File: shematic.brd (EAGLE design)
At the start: 99 x 50.5 mm, 15 parts, among them Y1 16MHZ

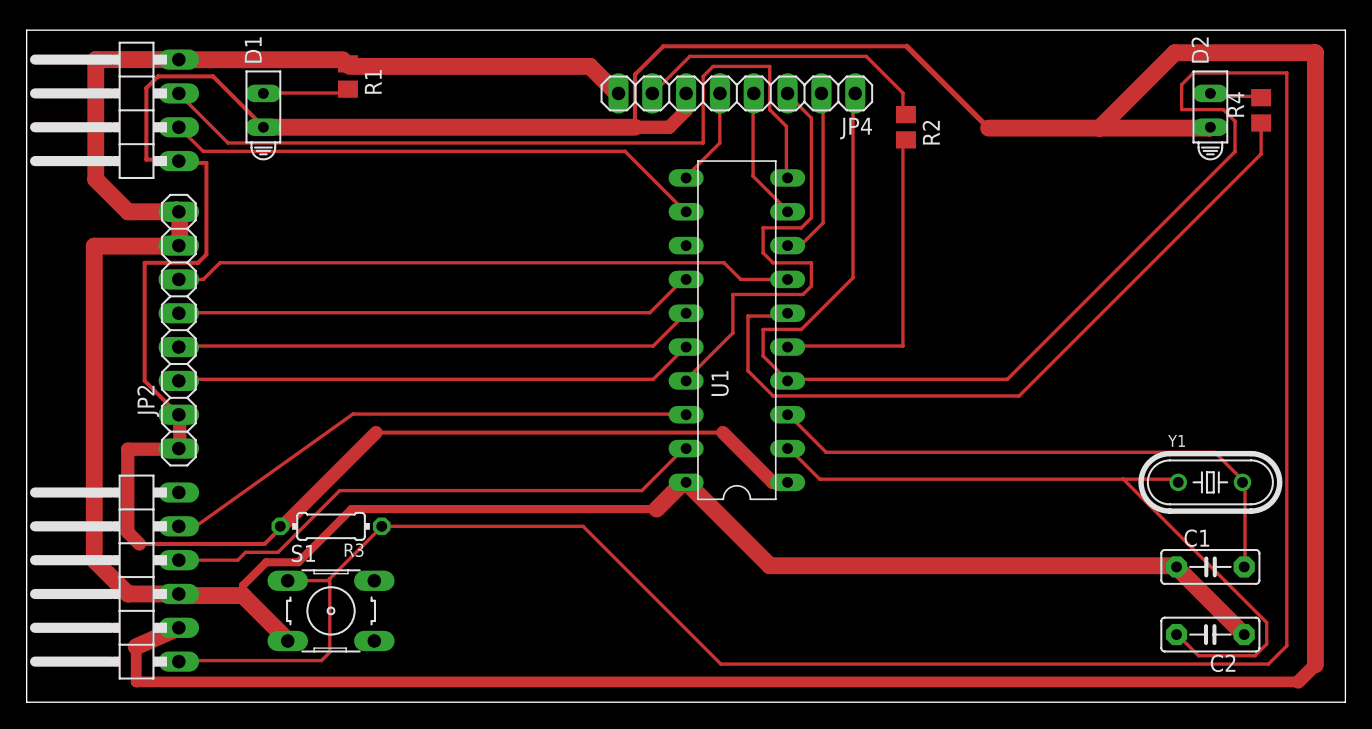
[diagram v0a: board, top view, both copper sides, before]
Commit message: set taller routes width
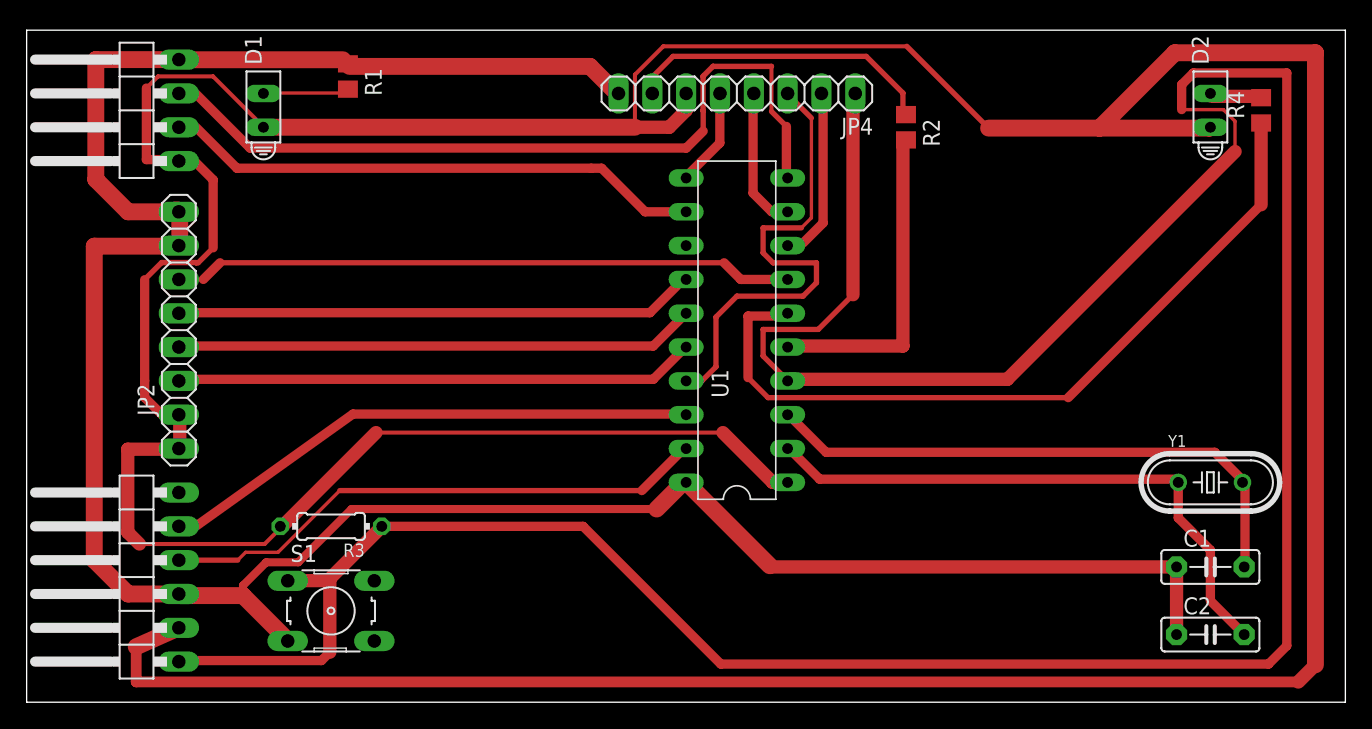
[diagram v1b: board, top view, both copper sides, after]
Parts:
- turned C2 to 0 degrees
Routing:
- net N$2: track 55.0 -> 43.9 mm
- net RC4: track 56.4 -> 59.0 mm
- net GND: track 190.2 -> 188.1 mm
- net DC: track 35.7 -> 36.7 mm
- net VPP: track 226.2 -> 226.9 mm
- net N$5: track 22.9 -> 23.6 mm
- net SDO: track 9.97 -> 10.7 mm

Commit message: fix some wires
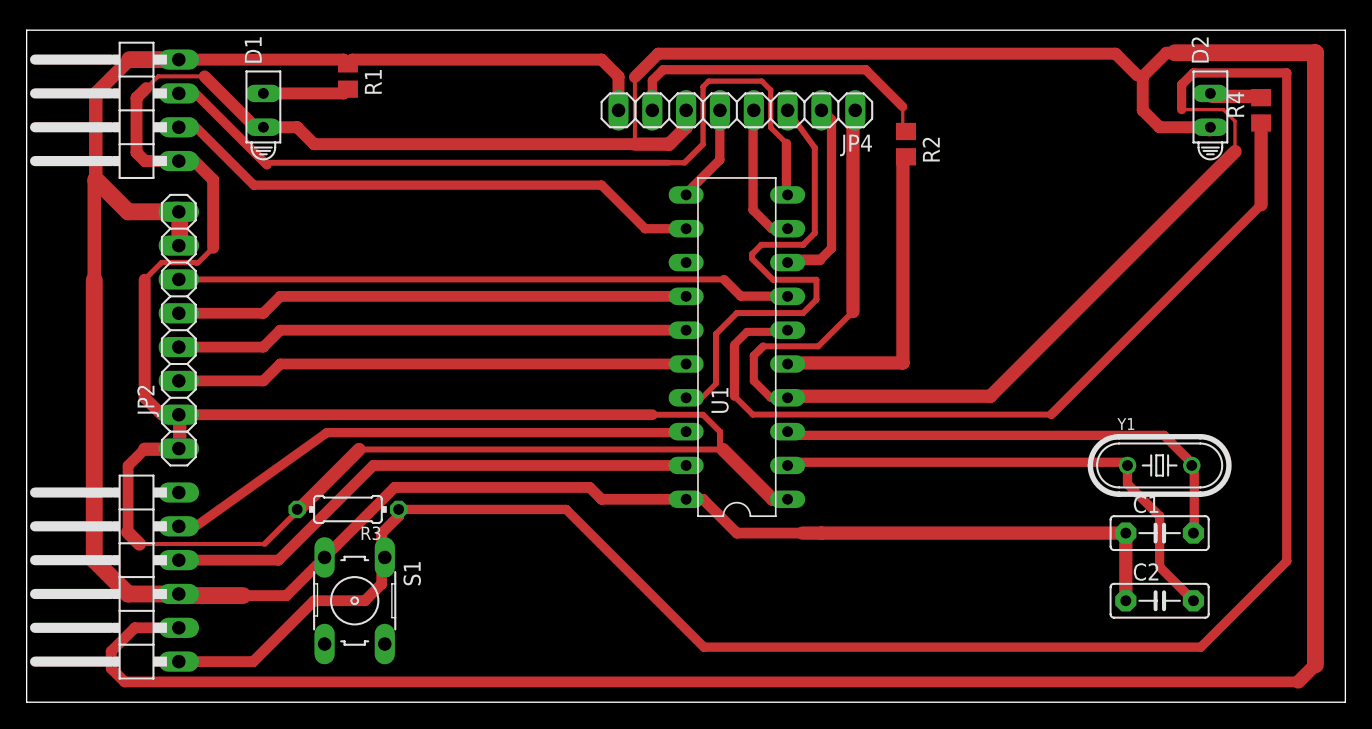
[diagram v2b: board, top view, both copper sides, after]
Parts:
- moved C1 4.58 mm to (85.1, 12.7)
- moved C2 4.58 mm to (85.1, 7.62)
- moved Y1 4.02 mm to (85.1, 17.8)
- moved S1 1.93 mm to (24.6, 7.62), turned to 270 degrees
- moved R3 1.80 mm to (24.1, 14.5)
- moved R2 1.27 mm to (66.0, 41.9)
- moved U1 1.27 mm to (53.3, 26.7)
- moved JP4 1.27 mm to (53.3, 44.5)
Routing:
- net +3V3: track 356.5 -> 399.8 mm
- net GND: track 188.1 -> 179.3 mm
- net N$2: track 43.9 -> 37.9 mm
- net N$1: track 42.9 -> 37.0 mm
- net VPP: track 226.9 -> 221.8 mm
- net RC4: track 59.0 -> 61.4 mm
- net N$5: track 23.6 -> 24.9 mm
- net SS: track 13.2 -> 14.4 mm
- net DC: track 36.7 -> 37.6 mm
- net N$3: track 6.46 -> 7.19 mm
- net RC0: track 39.2 -> 38.6 mm
- net RC1: track 39.2 -> 38.6 mm
- net RX: track 40.7 -> 41.3 mm
- net RC2: track 39.1 -> 38.6 mm
- net RC3: track 46.8 -> 46.2 mm

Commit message: mounting holes
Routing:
- net +3V3: track 399.8 -> 400.6 mm

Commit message: fix warnings
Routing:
- net GND: track 179.3 -> 177.7 mm
- net N$3: track 7.19 -> 6.48 mm
